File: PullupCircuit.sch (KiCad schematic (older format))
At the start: 4 parts, among them U3 DMC2700

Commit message: RTC update
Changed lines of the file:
@@
 EESchema Schematic File Version 2
+LIBS:maxim
 LIBS:dmc2700
 LIBS:iso1540
@@
 AR Path="/59B46FD6/59B40F2D/59B3FFA1" Ref="U9"  Part="1"
 AR Path="/59B46FD6/59B419E1/59B3FFA1" Ref="U10"  Part="1"
-F 0 "U3" H 4990 2110 50  0000 L CNN
+F 0 "U10" H 4990 2110 50  0000 L CNN
 F 1 "DMC2700" H 4990 2935 50  0000 L CNN
 F 2 "TO_SOT_Packages_SMD:SOT-23-6_Handsoldering" H 5450 2475 50  0001 L CIN
@@
 AR Path="/59B46FD6/59B40F2D/59B4002B" Ref="R28"  Part="1"
 AR Path="/59B46FD6/59B419E1/59B4002B" Ref="R31"  Part="1"
-F 0 "R12" V 5880 2250 50  0000 C CNN
+F 0 "R31" V 5880 2250 50  0000 C CNN
 F 1 "200R" V 5800 2250 50  0000 C CNN
 F 2 "Resistors_SMD:R_1206_HandSoldering" V 5730 2250 50  0001 C CNN
@@
 	6000 2250 5950 2250
 $Comp
-L +5V #PWR042
+L +5V #PWR049
 U 1 1 59B40098
 P 5700 2500
-AR Path="/59A988EA/59B40F2D/59B40098" Ref="#PWR042"  Part="1"
-AR Path="/59A988EA/59B419E1/59B40098" Ref="#PWR046"  Part="1"
-AR Path="/59B431E3/59B40F2D/59B40098" Ref="#PWR066"  Part="1"
-AR Path="/59B431E3/59B419E1/59B40098" Ref="#PWR070"  Part="1"
-AR Path="/59B46FD6/59B40F2D/59B40098" Ref="#PWR090"  Part="1"
-AR Path="/59B46FD6/59B419E1/59B40098" Ref="#PWR094"  Part="1"
-F 0 "#PWR042" H 5700 2350 50  0001 C CNN
+AR Path="/59A988EA/59B40F2D/59B40098" Ref="#PWR049"  Part="1"
+AR Path="/59A988EA/59B419E1/59B40098" Ref="#PWR053"  Part="1"
+AR Path="/59B431E3/59B40F2D/59B40098" Ref="#PWR073"  Part="1"
+AR Path="/59B431E3/59B419E1/59B40098" Ref="#PWR077"  Part="1"
+AR Path="/59B46FD6/59B40F2D/59B40098" Ref="#PWR097"  Part="1"
+AR Path="/59B46FD6/59B419E1/59B40098" Ref="#PWR0101"  Part="1"
+F 0 "#PWR0101" H 5700 2350 50  0001 C CNN
 F 1 "+5V" H 5700 2640 50  0000 C CNN
 F 2 "" H 5700 2500 50  0001 C CNN
@@
 $EndComp
 $Comp
-L GND #PWR043
+L GND #PWR050
 U 1 1 59B400B7
 P 5650 2900
-AR Path="/59A988EA/59B40F2D/59B400B7" Ref="#PWR043"  Part="1"
-AR Path="/59A988EA/59B419E1/59B400B7" Ref="#PWR047"  Part="1"
-AR Path="/59B431E3/59B40F2D/59B400B7" Ref="#PWR067"  Part="1"
-AR Path="/59B431E3/59B419E1/59B400B7" Ref="#PWR071"  Part="1"
-AR Path="/59B46FD6/59B40F2D/59B400B7" Ref="#PWR091"  Part="1"
-AR Path="/59B46FD6/59B419E1/59B400B7" Ref="#PWR095"  Part="1"
-F 0 "#PWR043" H 5650 2650 50  0001 C CNN
+AR Path="/59A988EA/59B40F2D/59B400B7" Ref="#PWR050"  Part="1"
+AR Path="/59A988EA/59B419E1/59B400B7" Ref="#PWR054"  Part="1"
+AR Path="/59B431E3/59B40F2D/59B400B7" Ref="#PWR074"  Part="1"
+AR Path="/59B431E3/59B419E1/59B400B7" Ref="#PWR078"  Part="1"
+AR Path="/59B46FD6/59B40F2D/59B400B7" Ref="#PWR098"  Part="1"
+AR Path="/59B46FD6/59B419E1/59B400B7" Ref="#PWR0102"  Part="1"
+F 0 "#PWR0102" H 5650 2650 50  0001 C CNN
 F 1 "GND" H 5650 2750 50  0000 C CNN
 F 2 "" H 5650 2900 50  0001 C CNN
@@
 AR Path="/59B46FD6/59B40F2D/59B400E4" Ref="R29"  Part="1"
 AR Path="/59B46FD6/59B419E1/59B400E4" Ref="R32"  Part="1"
-F 0 "R13" V 4630 2400 50  0000 C CNN
+F 0 "R32" V 4630 2400 50  0000 C CNN
 F 1 "10k" V 4550 2400 50  0000 C CNN
 F 2 "Resistors_SMD:R_0603_HandSoldering" V 4480 2400 50  0001 C CNN
@@
 Connection ~ 4750 2400
 $Comp
-L +5V #PWR044
+L +5V #PWR051
 U 1 1 59B4011D
 P 4350 2400
-AR Path="/59A988EA/59B40F2D/59B4011D" Ref="#PWR044"  Part="1"
-AR Path="/59A988EA/59B419E1/59B4011D" Ref="#PWR048"  Part="1"
-AR Path="/59B431E3/59B40F2D/59B4011D" Ref="#PWR068"  Part="1"
-AR Path="/59B431E3/59B419E1/59B4011D" Ref="#PWR072"  Part="1"
-AR Path="/59B46FD6/59B40F2D/59B4011D" Ref="#PWR092"  Part="1"
-AR Path="/59B46FD6/59B419E1/59B4011D" Ref="#PWR096"  Part="1"
-F 0 "#PWR044" H 4350 2250 50  0001 C CNN
+AR Path="/59A988EA/59B40F2D/59B4011D" Ref="#PWR051"  Part="1"
+AR Path="/59A988EA/59B419E1/59B4011D" Ref="#PWR055"  Part="1"
+AR Path="/59B431E3/59B40F2D/59B4011D" Ref="#PWR075"  Part="1"
+AR Path="/59B431E3/59B419E1/59B4011D" Ref="#PWR079"  Part="1"
+AR Path="/59B46FD6/59B40F2D/59B4011D" Ref="#PWR099"  Part="1"
+AR Path="/59B46FD6/59B419E1/59B4011D" Ref="#PWR0103"  Part="1"
+F 0 "#PWR0103" H 4350 2250 50  0001 C CNN
 F 1 "+5V" H 4350 2540 50  0000 C CNN
 F 2 "" H 4350 2400 50  0001 C CNN
@@
 AR Path="/59B46FD6/59B40F2D/59B4013F" Ref="R30"  Part="1"
 AR Path="/59B46FD6/59B419E1/59B4013F" Ref="R33"  Part="1"
-F 0 "R14" V 4880 2950 50  0000 C CNN
+F 0 "R33" V 4880 2950 50  0000 C CNN
 F 1 "10k" V 4800 2950 50  0000 C CNN
 F 2 "Resistors_SMD:R_0603_HandSoldering" V 4730 2950 50  0001 C CNN
@@
 	4800 3100 4800 3150
 $Comp
-L GND #PWR045
+L GND #PWR052
 U 1 1 59B401E2
 P 4800 3150
-AR Path="/59A988EA/59B40F2D/59B401E2" Ref="#PWR045"  Part="1"
-AR Path="/59A988EA/59B419E1/59B401E2" Ref="#PWR049"  Part="1"
-AR Path="/59B431E3/59B40F2D/59B401E2" Ref="#PWR069"  Part="1"
-AR Path="/59B431E3/59B419E1/59B401E2" Ref="#PWR073"  Part="1"
-AR Path="/59B46FD6/59B40F2D/59B401E2" Ref="#PWR093"  Part="1"
-AR Path="/59B46FD6/59B419E1/59B401E2" Ref="#PWR097"  Part="1"
-F 0 "#PWR045" H 4800 2900 50  0001 C CNN
+AR Path="/59A988EA/59B40F2D/59B401E2" Ref="#PWR052"  Part="1"
+AR Path="/59A988EA/59B419E1/59B401E2" Ref="#PWR056"  Part="1"
+AR Path="/59B431E3/59B40F2D/59B401E2" Ref="#PWR076"  Part="1"
+AR Path="/59B431E3/59B419E1/59B401E2" Ref="#PWR080"  Part="1"
+AR Path="/59B46FD6/59B40F2D/59B401E2" Ref="#PWR0100"  Part="1"
+AR Path="/59B46FD6/59B419E1/59B401E2" Ref="#PWR0104"  Part="1"
+F 0 "#PWR0104" H 4800 2900 50  0001 C CNN
 F 1 "GND" H 4800 3000 50  0000 C CNN
 F 2 "" H 4800 3150 50  0001 C CNN

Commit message: Cleanups
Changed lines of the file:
@@
 AR Path="/59B46FD6/59B40F2D/59B3FFA1" Ref="U9"  Part="1"
 AR Path="/59B46FD6/59B419E1/59B3FFA1" Ref="U10"  Part="1"
-F 0 "U10" H 4990 2110 50  0000 L CNN
+F 0 "U9" H 4990 2110 50  0000 L CNN
 F 1 "DMC2700" H 4990 2935 50  0000 L CNN
 F 2 "TO_SOT_Packages_SMD:SOT-23-6_Handsoldering" H 5450 2475 50  0001 L CIN
@@
 AR Path="/59B46FD6/59B40F2D/59B4002B" Ref="R28"  Part="1"
 AR Path="/59B46FD6/59B419E1/59B4002B" Ref="R31"  Part="1"
-F 0 "R31" V 5880 2250 50  0000 C CNN
+F 0 "R28" V 5880 2250 50  0000 C CNN
 F 1 "200R" V 5800 2250 50  0000 C CNN
 F 2 "Resistors_SMD:R_1206_HandSoldering" V 5730 2250 50  0001 C CNN
@@
 AR Path="/59B46FD6/59B40F2D/59B400E4" Ref="R29"  Part="1"
 AR Path="/59B46FD6/59B419E1/59B400E4" Ref="R32"  Part="1"
-F 0 "R32" V 4630 2400 50  0000 C CNN
+F 0 "R29" V 4630 2400 50  0000 C CNN
 F 1 "10k" V 4550 2400 50  0000 C CNN
 F 2 "Resistors_SMD:R_0603_HandSoldering" V 4480 2400 50  0001 C CNN
@@
 AR Path="/59B46FD6/59B40F2D/59B4013F" Ref="R30"  Part="1"
 AR Path="/59B46FD6/59B419E1/59B4013F" Ref="R33"  Part="1"
-F 0 "R33" V 4880 2950 50  0000 C CNN
+F 0 "R30" V 4880 2950 50  0000 C CNN
 F 1 "10k" V 4800 2950 50  0000 C CNN
 F 2 "Resistors_SMD:R_0603_HandSoldering" V 4730 2950 50  0001 C CNN

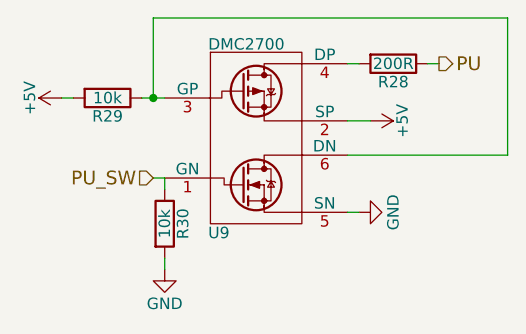
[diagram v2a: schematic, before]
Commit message: Cleanup teensy schematic and remove old custom.lib
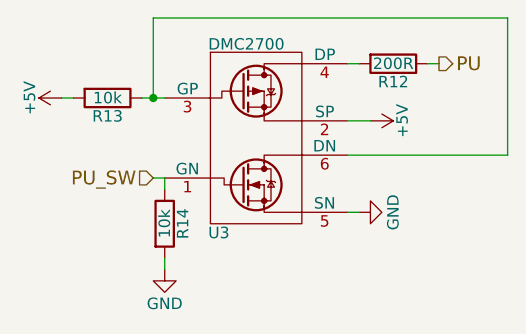
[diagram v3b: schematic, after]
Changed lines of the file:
@@
 EESchema Schematic File Version 2
+LIBS:teensy36_no-center
+LIBS:ldd-1000h
 LIBS:maxim
 LIBS:dmc2700
 LIBS:iso1540
 LIBS:74lvc
-LIBS:custom
 LIBS:ledflashcontroller-rescue
 LIBS:power
@@
 $Descr A4 11693 8268
 encoding utf-8
-Sheet 10 10
+Sheet 3 10
 Title ""
 Date ""
@@
 AR Path="/59B46FD6/59B40F2D/59B3FFA1" Ref="U9"  Part="1"
 AR Path="/59B46FD6/59B419E1/59B3FFA1" Ref="U10"  Part="1"
-F 0 "U9" H 4990 2110 50  0000 L CNN
+F 0 "U3" H 4990 2110 50  0000 L CNN
 F 1 "DMC2700" H 4990 2935 50  0000 L CNN
 F 2 "TO_SOT_Packages_SMD:SOT-23-6_Handsoldering" H 5450 2475 50  0001 L CIN
@@
 AR Path="/59B46FD6/59B40F2D/59B4002B" Ref="R28"  Part="1"
 AR Path="/59B46FD6/59B419E1/59B4002B" Ref="R31"  Part="1"
-F 0 "R28" V 5880 2250 50  0000 C CNN
+F 0 "R12" V 5880 2250 50  0000 C CNN
 F 1 "200R" V 5800 2250 50  0000 C CNN
 F 2 "Resistors_SMD:R_1206_HandSoldering" V 5730 2250 50  0001 C CNN
@@
 AR Path="/59B46FD6/59B40F2D/59B40098" Ref="#PWR097"  Part="1"
 AR Path="/59B46FD6/59B419E1/59B40098" Ref="#PWR0101"  Part="1"
-F 0 "#PWR0101" H 5700 2350 50  0001 C CNN
+F 0 "#PWR049" H 5700 2350 50  0001 C CNN
 F 1 "+5V" H 5700 2640 50  0000 C CNN
 F 2 "" H 5700 2500 50  0001 C CNN
@@
 AR Path="/59B46FD6/59B40F2D/59B400B7" Ref="#PWR098"  Part="1"
 AR Path="/59B46FD6/59B419E1/59B400B7" Ref="#PWR0102"  Part="1"
-F 0 "#PWR0102" H 5650 2650 50  0001 C CNN
+F 0 "#PWR050" H 5650 2650 50  0001 C CNN
 F 1 "GND" H 5650 2750 50  0000 C CNN
 F 2 "" H 5650 2900 50  0001 C CNN
@@
 AR Path="/59B46FD6/59B40F2D/59B400E4" Ref="R29"  Part="1"
 AR Path="/59B46FD6/59B419E1/59B400E4" Ref="R32"  Part="1"
-F 0 "R29" V 4630 2400 50  0000 C CNN
+F 0 "R13" V 4630 2400 50  0000 C CNN
 F 1 "10k" V 4550 2400 50  0000 C CNN
 F 2 "Resistors_SMD:R_0603_HandSoldering" V 4480 2400 50  0001 C CNN
@@
 AR Path="/59B46FD6/59B40F2D/59B4011D" Ref="#PWR099"  Part="1"
 AR Path="/59B46FD6/59B419E1/59B4011D" Ref="#PWR0103"  Part="1"
-F 0 "#PWR0103" H 4350 2250 50  0001 C CNN
+F 0 "#PWR051" H 4350 2250 50  0001 C CNN
 F 1 "+5V" H 4350 2540 50  0000 C CNN
 F 2 "" H 4350 2400 50  0001 C CNN
@@
 AR Path="/59B46FD6/59B40F2D/59B4013F" Ref="R30"  Part="1"
 AR Path="/59B46FD6/59B419E1/59B4013F" Ref="R33"  Part="1"
-F 0 "R30" V 4880 2950 50  0000 C CNN
+F 0 "R14" V 4880 2950 50  0000 C CNN
 F 1 "10k" V 4800 2950 50  0000 C CNN
 F 2 "Resistors_SMD:R_0603_HandSoldering" V 4730 2950 50  0001 C CNN
@@
 AR Path="/59B46FD6/59B40F2D/59B401E2" Ref="#PWR0100"  Part="1"
 AR Path="/59B46FD6/59B419E1/59B401E2" Ref="#PWR0104"  Part="1"
-F 0 "#PWR0104" H 4800 2900 50  0001 C CNN
+F 0 "#PWR052" H 4800 2900 50  0001 C CNN
 F 1 "GND" H 4800 3000 50  0000 C CNN
 F 2 "" H 4800 3150 50  0001 C CNN
